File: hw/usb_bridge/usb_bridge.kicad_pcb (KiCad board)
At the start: 2 copper layers, 51 x 31 mm, 74 parts, among them J1 USB_C_Receptacle_USB2.0_14P, J2 DE9, J3 SWD, J4 BOOT, U1 CH340E, U2 MAX485E, U3 CH334R, U5 MCP1754S-3302xCB, U6 TJA1051T-3, U7 STM32G0B1CBT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

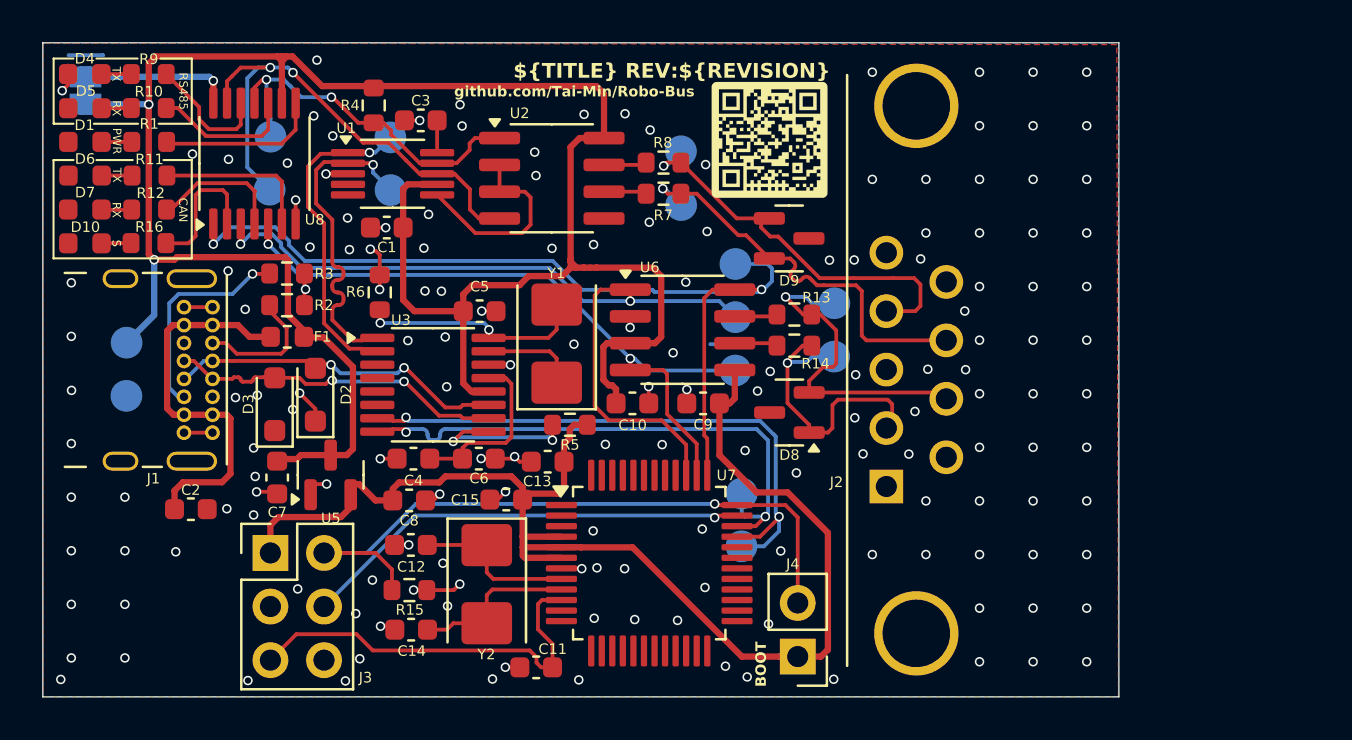
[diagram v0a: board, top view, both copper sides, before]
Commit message: usb_bridge: Major LED fixes, replace USB-C protection circuit, add RS485 pullups, add mounting holes
Signed-off-by: Mateusz Pajak <22417805+Tai-Min@users.noreply.github.com>
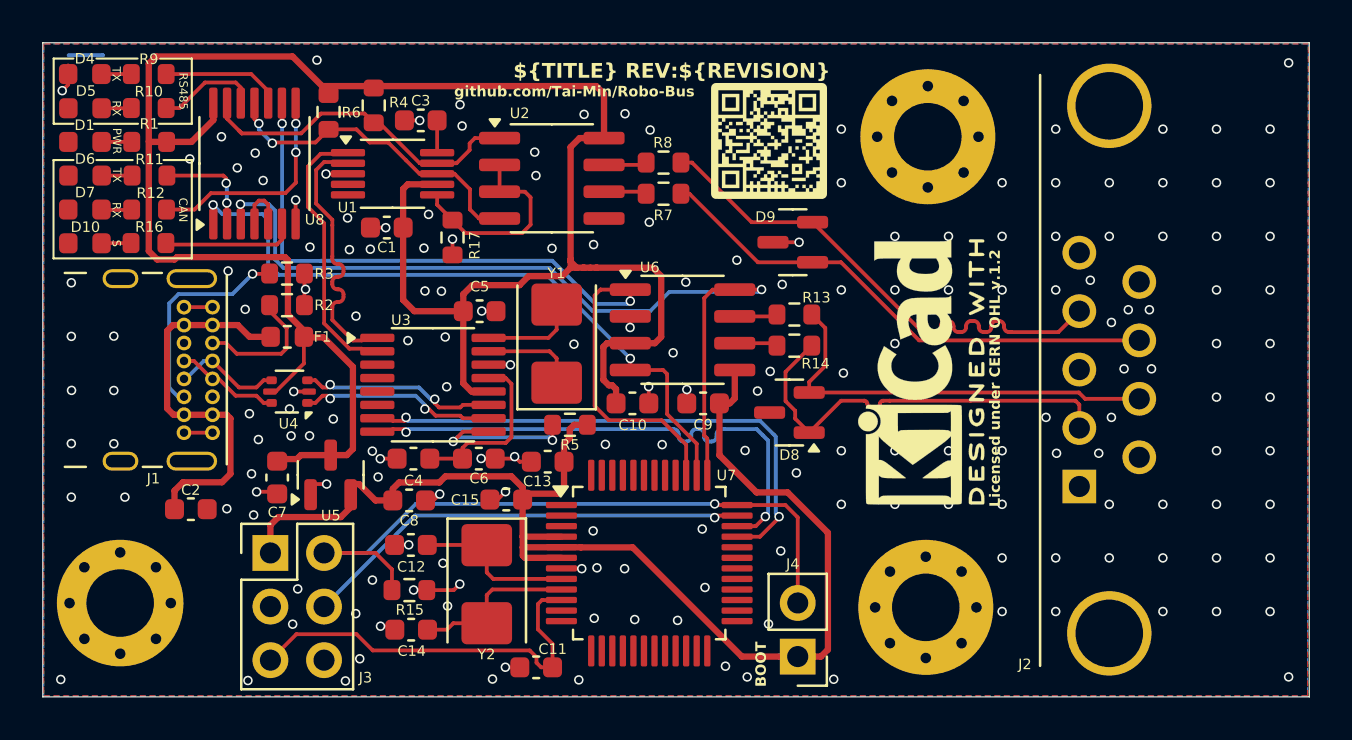
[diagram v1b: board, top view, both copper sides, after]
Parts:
- removed D2, D3: PESD5V0S1BA, Diode_SMD:D_SOD-323_HandSoldering
- removed JP1: Jumper_2_Bridged, Jumper:SolderJumper-2_P1.3mm_Bridged_RoundedPad1.0x1.5mm
- removed TP1, TP10, TP11, TP12, TP13, TP14, TP15, TP16, TP2, TP4, TP5, TP6, TP7, TP8, TP9: TestPoint, TestPoint:TestPoint_Pad_D1.5mm
- added H1: MountingHole_Pad, MountingHole:MountingHole_3.2mm_M3_Pad_Via, F.Cu at (168.4, 91.0)
- added H2: MountingHole_Pad, MountingHole:MountingHole_3.2mm_M3_Pad_Via, F.Cu at (130.1, 113.1)
- added H3: MountingHole_Pad, MountingHole:MountingHole_3.2mm_M3_Pad_Via, F.Cu at (168.3, 113.3)
- added R17: 10K, Resistor_SMD:R_0603_1608Metric, F.Cu at (145.9, 95.8)
- added U4: USBLC6-2P6, Package_TO_SOT_SMD:SOT-666, F.Cu at (138.2, 103.1)
- R6: value 0R -> 10K
- REF**: moved to F.Cu
- moved REF** 16.1 mm to (183.1, 113.5)
- moved REF** 9.55 mm to (168.1, 102.2), turned to 90 degrees
- moved J2 9.15 mm to (175.6, 107.6)
- moved R6 8.89 mm to (140.0, 89.8), turned to -90 degrees
- moved D9 0.25 mm to (162.0, 96.0), turned to 180 degrees
- moved G*** 0.06 mm to (160.9, 91.7)
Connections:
- D9 pad 1: /MODBUS- -> /MODBUS+
- D9 pad 2: /MODBUS+ -> /MODBUS-
- J1 pad A6: /D+ -> /DP
- J1 pad A7: /D- -> /DN
- J1 pad B6: /D+ -> /DP
- J1 pad B7: /D- -> /DN
- R1 pad 2: Net-(R1-Pad2) -> +5V
- R6 pad 1: Net-(U3-XI) -> +5V
- R6 pad 2: GND -> /RS_TX
- U8 pad 1: /C_S -> /C_RX
- U8 pad 10: Net-(R10-Pad2) -> Net-(R9-Pad2)
- U8 pad 11: /RS_RX -> /RS_TX
- U8 pad 12: Net-(R9-Pad2) -> Net-(R10-Pad2)
- U8 pad 13: /RS_TX -> /RS_RX
- U8 pad 14: /LED_PWR -> +5V
- U8 pad 2: Net-(R16-Pad2) -> Net-(R11-Pad2)
- U8 pad 3: /C_TX -> /C_S
- U8 pad 4: Net-(R12-Pad2) -> Net-(U8-Pad4)
- U8 pad 5: /C_RX -> Net-(U8-Pad4)
- U8 pad 6: Net-(R11-Pad2) -> Net-(R16-Pad2)
- U8 pad 8: Net-(R1-Pad2) -> Net-(R12-Pad2)
- U8 pad 9: +5V -> /C_TX
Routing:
- net /RS_TX: track 24.8 -> 15.6 mm
- net Net-(R1-Pad2): track 7.69 -> 0.00 mm
- net /LED_PWR: track 7.20 -> 0.00 mm, vias 1 -> 0
- net /D-: track 16.3 -> 9.39 mm
- net /D+: track 15.8 -> 9.39 mm
- net Net-(U3-XI): track 10.9 -> 4.60 mm, vias 2 -> 0
- net /CAN-: track 14.4 -> 20.0 mm, vias 1 -> 0
- net /DP: track 0.00 -> 5.16 mm
- net /MODBUS-: track 19.4 -> 24.5 mm, vias 1 -> 0
- net /MODBUS+: track 19.6 -> 24.6 mm, vias 1 -> 0
- net /DN: track 0.00 -> 4.97 mm
- net Net-(R12-Pad2): track 6.77 -> 11.0 mm, vias 0 -> 2
- net /CAN+: track 15.9 -> 20.0 mm, vias 1 -> 0
- net GND: track 34.0 -> 30.5 mm, vias 164 -> 183
- net /D_RS-: track 15.7 -> 12.9 mm, vias 1 -> 0
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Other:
- board size 51 x 31 mm -> 60 x 31 mm
- board text removed: "5V"
- board text removed: "D+"
- board text removed: "GND"
- board text removed: "LED_PWR"

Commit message: Remove residual silkscreen from the bottom, replace LED resistor to 10K
Signed-off-by: Tai-Min <22417805+Tai-Min@users.noreply.github.com>
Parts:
- R1: value 1K -> 10K
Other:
- board text removed: "+"
- board text removed: "-"
- board text removed: "D-"
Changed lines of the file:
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@@
 		)
 	)
-	(property "REVISION" "1.0.1d")
+	(property "REVISION" "1.0.1rc")
 	(property "TITLE" "USB <-> CAN / RS485 ADAPTER")
 	(net 0 "")
@@
 			)
 		)
-		(property "Value" "1K"
+		(property "Value" "10K"
 			(at 0 1.43 0)
 			(layer "F.Fab")
@@
 			)
 		)
-		(property "LCSC Part #" "C22548"
+		(property "LCSC Part #" "C98220"
 			(at 0 0 0)
 			(unlocked yes)
@@
 			)
 		)
-		(property "Description" "Unpolarized capacitor"
+		(property "Description" "50V"
 			(at 0 0 0)
 			(layer "F.Fab")
@@
 			)
 		)
-		(property "Description" "Unpolarized capacitor"
+		(property "Description" "50V"
 			(at 0 0 0)
 			(layer "F.Fab")
@@
 		)
 	)
-	(gr_text "D-"
-		(at 141.87 93.53 90)
-		(layer "B.SilkS")
-		(effects
-			(font
-				(size 0.5 0.5)
-				(thickness 0.125)
-				(bold yes)
-			)
-			(justify bottom mirror)
-		)
-	)
-	(gr_text "+"
-		(at 155.52 94.22 90)
-		(layer "B.SilkS")
-		(effects
-			(font
-				(size 0.5 0.5)
-				(thickness 0.125)
-				(bold yes)
-			)
-			(justify bottom mirror)
-		)
-	)
-	(gr_text "-"
-		(at 155.54 91.65 90)
-		(layer "B.SilkS")
-		(effects
-			(font
-				(size 0.5 0.5)
-				(thickness 0.125)
-				(bold yes)
-			)
-			(justify bottom mirror)
-		)
-	)
-	(gr_text "+"
-		(at 162.86 98.91 90)
-		(layer "B.SilkS")
-		(effects
-			(font
-				(size 0.5 0.5)
-				(thickness 0.125)
-				(bold yes)
-			)
-			(justify bottom mirror)
-		)
-	)
-	(gr_text "S"
-		(at 158.14 97 90)
-		(layer "B.SilkS")
-		(effects
-			(font
-				(size 0.5 0.5)
-				(thickness 0.125)
-				(bold yes)
-			)
-			(justify bottom mirror)
-		)
-	)
-	(gr_text "-"
-		(at 162.84 101.48 90)
-		(layer "B.SilkS")
-		(effects
-			(font
-				(size 0.5 0.5)
-				(thickness 0.125)
-				(bold yes)
-			)
-			(justify bottom mirror)
-		)
-	)
